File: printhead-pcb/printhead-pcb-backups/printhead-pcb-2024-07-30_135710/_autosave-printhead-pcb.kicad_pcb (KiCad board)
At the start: 2 copper layers, 35 x 35 mm, 30 parts, among them J1 Power, J13 Steckverbinder_Male_1, J3 DATA, U1 PCA9615DP, U6 AP7361C-33E

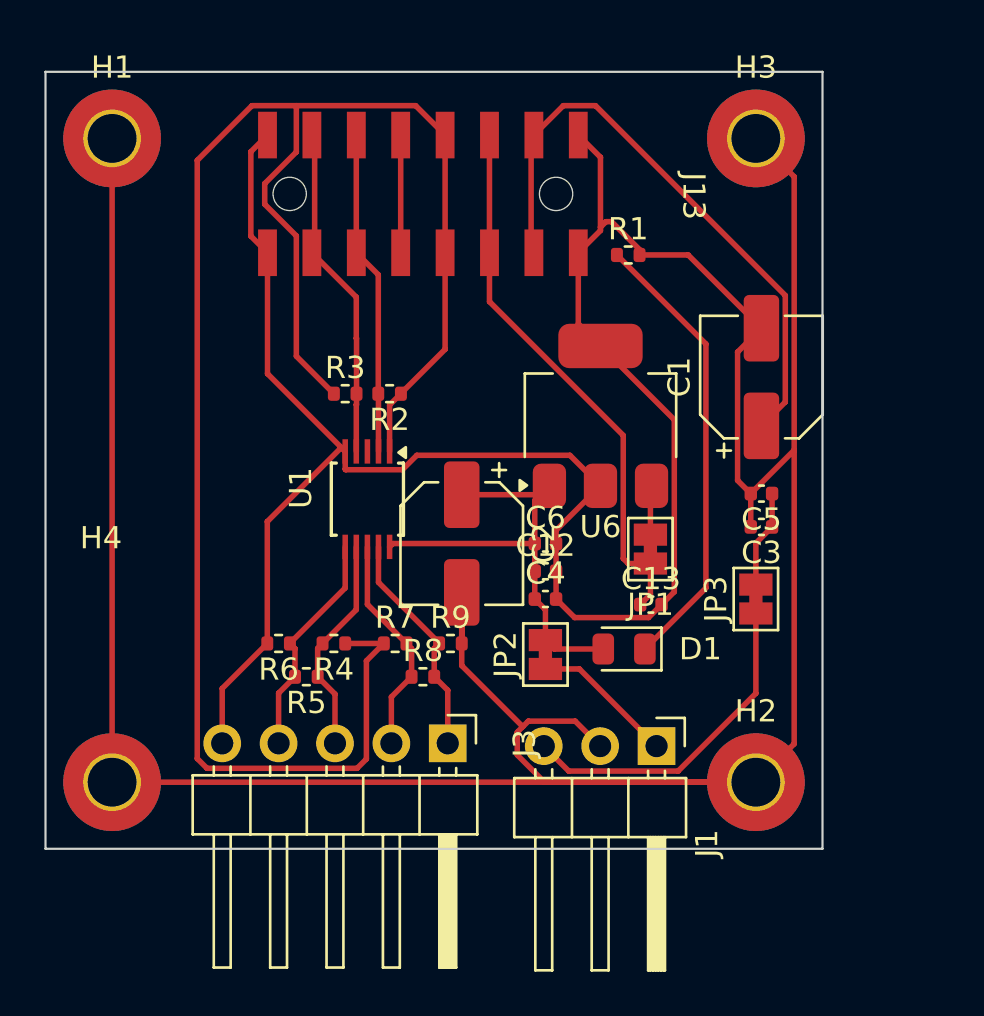
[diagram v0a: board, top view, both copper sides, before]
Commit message: version that almost has it but no matter how hard i try i cant seem to make all connections with just one layer, so ill have to use two layers
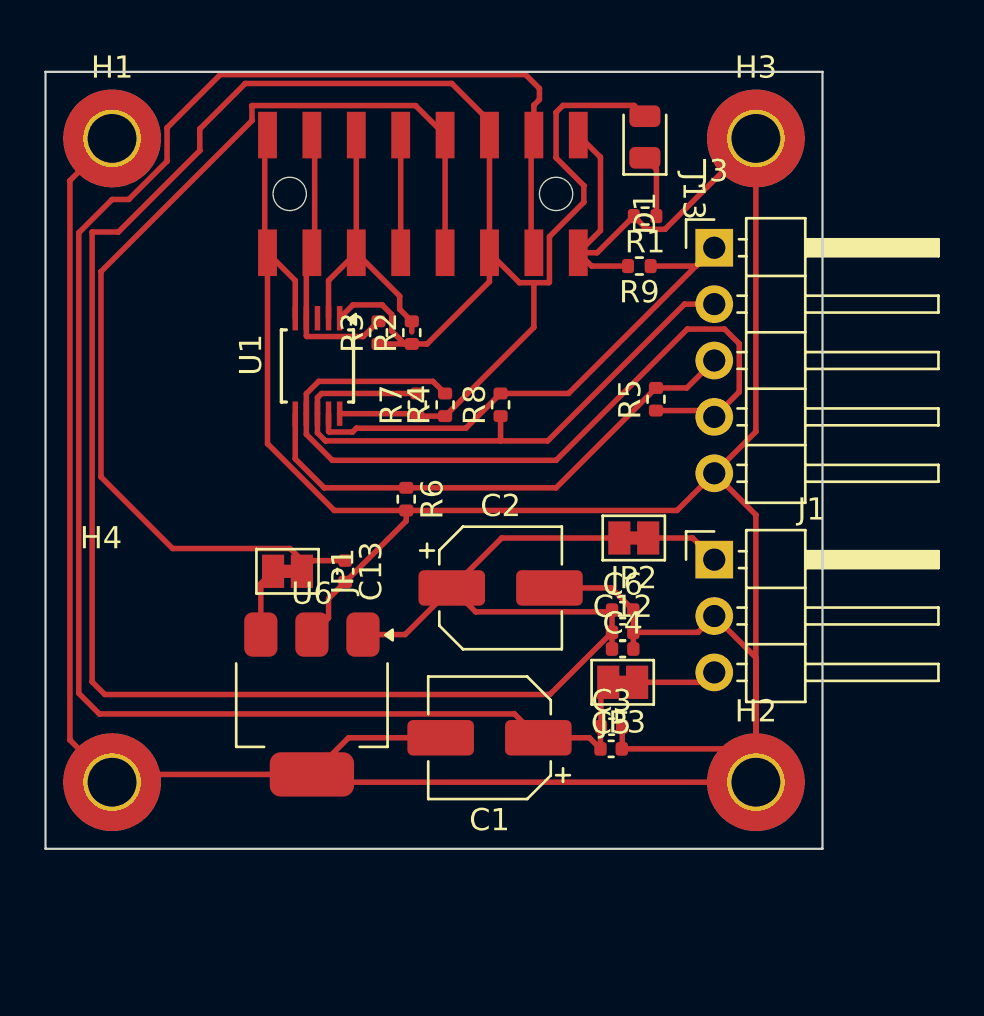
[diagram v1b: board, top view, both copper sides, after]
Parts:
- moved J3 25.3 mm to (245.6, 72.9), turned to 0 degrees
- moved D1 23.1 mm to (242.5, 67.9), turned to 90 degrees
- moved C1 20.4 mm to (235.5, 95.0), turned to 180 degrees
- moved R5 20.1 mm to (243.0, 79.8), turned to 90 degrees
- moved R9 19.0 mm to (242.2, 73.8), turned to 180 degrees
- moved U6 18.4 mm to (227.5, 93.5), turned to -90 degrees
- moved JP1 16.4 mm to (226.4, 87.5), turned to 0 degrees
- moved C13 13.9 mm to (229.0, 87.5), turned to -90 degrees
- moved C5 13.3 mm to (241.0, 95.5), turned to 0 degrees
- moved R8 12.7 mm to (236.0, 80.0), turned to 90 degrees
- moved R4 11.9 mm to (233.5, 80.0), turned to 90 degrees
- moved C3 11.2 mm to (241.0, 94.5), turned to 0 degrees
- moved R7 10.8 mm to (232.2, 80.0), turned to 90 degrees
- moved J1 8.79 mm to (245.6, 87.0), turned to 0 degrees
- moved R6 8.68 mm to (231.8, 84.2), turned to -90 degrees
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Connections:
- J13 pad a3: +3V3 -> +5V
- J13 pad a4: +5V -> +3V3
- J13 pad b3: +3V3 -> +5V
- J13 pad b4: +5V -> +3V3
- J3 pad 3: unconnected-(J3-Pin_3-Pad3) -> DSCLM
- J3 pad 4: unconnected-(J3-Pin_4-Pad4) -> DSCLP
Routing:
- net +12V: track 31.5 -> 80.9 mm
- net +5V: track 106.0 -> 136.8 mm
- net GND: track 218.3 -> 189.5 mm
- net DSCLP: track 9.89 -> 37.7 mm
- net +3V3: track 24.9 -> 47.3 mm
- net DSDAP: track 10.1 -> 27.9 mm
- net Net-(D1-K): track 20.6 -> 2.84 mm
- net DSDAM: track 10.3 -> 24.8 mm
- net DSCLM: track 10.3 -> 23.8 mm
- net Net-(J1-Pin_3): track 15.1 -> 3.66 mm
- net Net-(J1-Pin_1): track 6.44 -> 3.38 mm
- net SCL: track 15.2 -> 12.8 mm
- net SDA: track 14.7 -> 13.4 mm
- net Net-(JP1-A): track 2.22 -> 3.08 mm
